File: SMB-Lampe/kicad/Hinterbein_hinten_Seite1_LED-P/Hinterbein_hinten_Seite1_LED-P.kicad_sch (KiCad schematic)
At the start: 10 parts, among them J1 Conn_01x01_Pin, J2 Conn_01x01_Pin, J3 Conn_01x01_Pin, J4 Conn_01x01_Pin, J5 Conn_01x01_Pin, J6 Conn_01x01_Pin

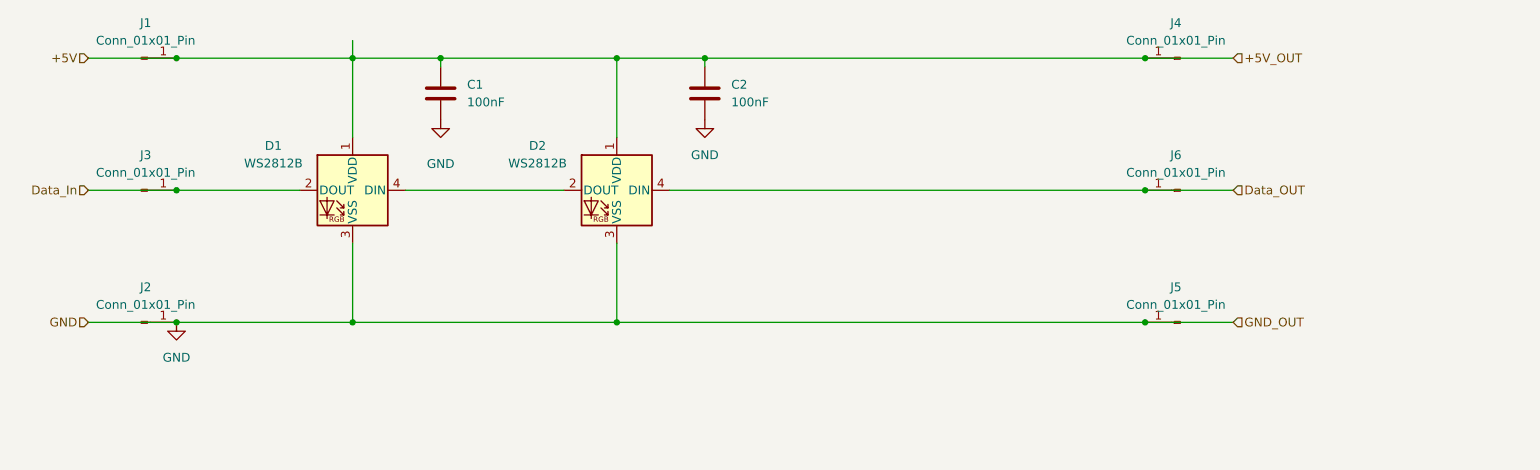
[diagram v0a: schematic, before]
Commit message: Hauptplatine skizziert
Bezeichner stimmen noch nicht
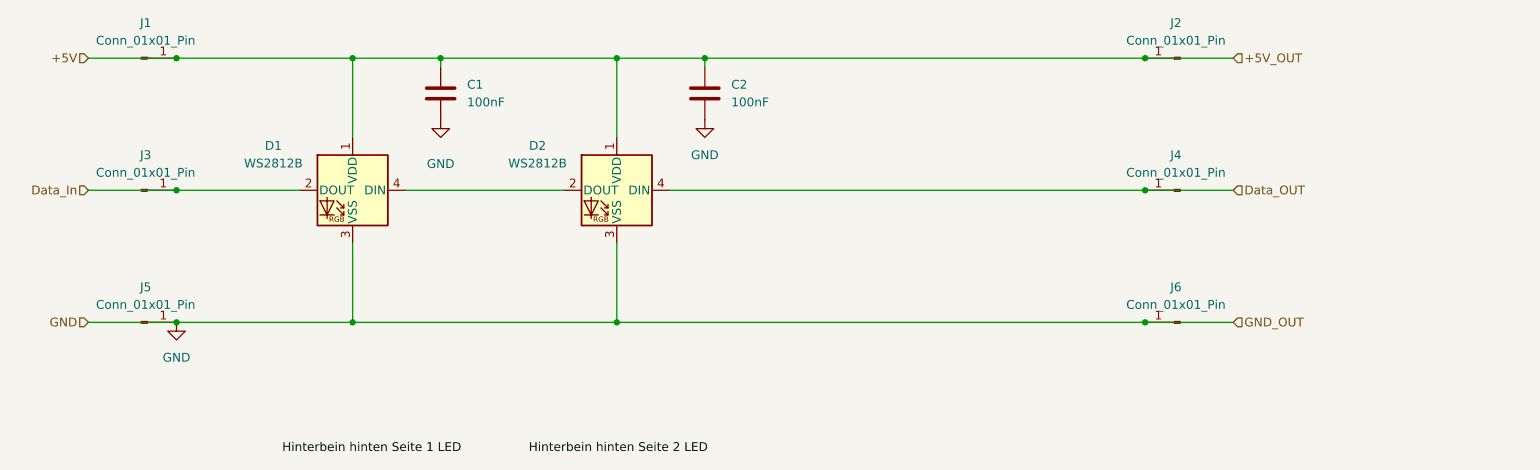
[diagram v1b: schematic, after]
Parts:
- renumbered J4 to J2, J6 to J4, J2 to J5, J5 to J6
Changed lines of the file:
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@@
 	(wire
 		(pts
-			(xy 63.5 22.86) (xy 63.5 25.4)
+			(xy 101.6 63.5) (xy 177.8 63.5)
 		)
 		(stroke
@@
 	(wire
 		(pts
-			(xy 101.6 63.5) (xy 177.8 63.5)
+			(xy 38.1 44.45) (xy 55.88 44.45)
 		)
 		(stroke
@@
 	(wire
 		(pts
-			(xy 38.1 44.45) (xy 55.88 44.45)
+			(xy 101.6 25.4) (xy 101.6 36.83)
 		)
 		(stroke
@@
 	(wire
 		(pts
-			(xy 101.6 25.4) (xy 101.6 36.83)
+			(xy 63.5 25.4) (xy 76.2 25.4)
 		)
 		(stroke
@@
 	(wire
 		(pts
-			(xy 63.5 25.4) (xy 76.2 25.4)
+			(xy 76.2 25.4) (xy 76.2 26.67)
 		)
 		(stroke
@@
 	(wire
 		(pts
-			(xy 76.2 25.4) (xy 76.2 26.67)
+			(xy 114.3 26.67) (xy 114.3 25.4)
 		)
 		(stroke
@@
 	(wire
 		(pts
-			(xy 114.3 26.67) (xy 114.3 25.4)
+			(xy 109.22 44.45) (xy 177.8 44.45)
 		)
 		(stroke
@@
 	(wire
 		(pts
-			(xy 109.22 44.45) (xy 177.8 44.45)
+			(xy 71.12 44.45) (xy 93.98 44.45)
 		)
 		(stroke
@@
 	(wire
 		(pts
-			(xy 71.12 44.45) (xy 93.98 44.45)
+			(xy 63.5 52.07) (xy 63.5 63.5)
 		)
 		(stroke
@@
 		)
 	)
-	(wire
-		(pts
-			(xy 63.5 52.07) (xy 63.5 63.5)
-		)
-		(stroke
-			(width 0)
-			(type default)
+	(label "Hinterbein hinten Seite 1 LED"
+		(at 53.34 82.55 0)
+		(effects
+			(font
+				(size 1.27 1.27)
+			)
+			(justify left bottom)
+		)
+	)
+	(label "Hinterbein hinten Seite 2 LED"
+		(at 88.9 82.55 0)
+		(effects
+			(font
+				(size 1.27 1.27)
+			)
+			(justify left bottom)
 		)
 	)
@@
 		(dnp no)
 		(fields_autoplaced yes)
-		(property "Reference" "J2"
+		(property "Reference" "J5"
 			(at 33.655 58.42 0)
 			(effects
@@
 		)
 		(instances
+			(project "SMB-Lampe"
+				(path "/4831ca1b-de6c-4f01-b2f4-c7955e9e85c5/5b746b9f-02d4-420a-904b-6236dfc25b23"
+					(reference "J5")
+					(unit 1)
+				)
+			)
 			(project ""
 				(path "/a4509e87-5503-4154-8e73-9784c4a4e9d8"
@@
 		(dnp no)
 		(fields_autoplaced yes)
-		(property "Reference" "#PWR0103"
+		(property "Reference" "#PWR05"
 			(at 38.1 69.85 0)
 			(effects
@@
 			(project ""
 				(path "/4831ca1b-de6c-4f01-b2f4-c7955e9e85c5/5b746b9f-02d4-420a-904b-6236dfc25b23"
-					(reference "#PWR04")
+					(reference "#PWR05")
 					(unit 1)
 				)
@@
 		)
 		(instances
+			(project "SMB-Lampe"
+				(path "/4831ca1b-de6c-4f01-b2f4-c7955e9e85c5/5b746b9f-02d4-420a-904b-6236dfc25b23"
+					(reference "J1")
+					(unit 1)
+				)
+			)
 			(project ""
 				(path "/a4509e87-5503-4154-8e73-9784c4a4e9d8"
@@
 			(project "SMB-Lampe"
 				(path "/4831ca1b-de6c-4f01-b2f4-c7955e9e85c5/5b746b9f-02d4-420a-904b-6236dfc25b23"
-					(reference "D3")
+					(reference "D2")
 					(unit 1)
 				)
@@
 		(dnp no)
 		(fields_autoplaced yes)
-		(property "Reference" "J4"
+		(property "Reference" "J2"
 			(at 182.245 20.32 0)
 			(effects
@@
 		)
 		(instances
+			(project "SMB-Lampe"
+				(path "/4831ca1b-de6c-4f01-b2f4-c7955e9e85c5/5b746b9f-02d4-420a-904b-6236dfc25b23"
+					(reference "J2")
+					(unit 1)
+				)
+			)
 			(project ""
 				(path "/a4509e87-5503-4154-8e73-9784c4a4e9d8"
@@
 		)
 		(instances
+			(project "SMB-Lampe"
+				(path "/4831ca1b-de6c-4f01-b2f4-c7955e9e85c5/5b746b9f-02d4-420a-904b-6236dfc25b23"
+					(reference "J3")
+					(unit 1)
+				)
+			)
 			(project ""
 				(path "/a4509e87-5503-4154-8e73-9784c4a4e9d8"
@@
 		(dnp no)
 		(fields_autoplaced yes)
-		(property "Reference" "J6"
+		(property "Reference" "J4"
 			(at 182.245 39.37 0)
 			(effects
@@
 		)
 		(instances
+			(project "SMB-Lampe"
+				(path "/4831ca1b-de6c-4f01-b2f4-c7955e9e85c5/5b746b9f-02d4-420a-904b-6236dfc25b23"
+					(reference "J4")
+					(unit 1)
+				)
+			)
 			(project ""
 				(path "/a4509e87-5503-4154-8e73-9784c4a4e9d8"
@@
 		(on_board yes)
 		(dnp no)
-		(property "Reference" "#PWR0101"
+		(property "Reference" "#PWR03"
 			(at 76.2 40.64 0)
 			(effects
@@
 		(dnp no)
 		(fields_autoplaced yes)
-		(property "Reference" "#PWR0102"
+		(property "Reference" "#PWR04"
 			(at 114.3 40.64 0)
 			(effects
@@
 			(project "SMB-Lampe"
 				(path "/4831ca1b-de6c-4f01-b2f4-c7955e9e85c5/5b746b9f-02d4-420a-904b-6236dfc25b23"
-					(reference "#PWR05")
+					(reference "#PWR04")
 					(unit 1)
 				)
@@
 		(dnp no)
 		(fields_autoplaced yes)
-		(property "Reference" "J5"
+		(property "Reference" "J6"
 			(at 182.245 58.42 0)
 			(effects
@@
 		)
 		(instances
+			(project "SMB-Lampe"
+				(path "/4831ca1b-de6c-4f01-b2f4-c7955e9e85c5/5b746b9f-02d4-420a-904b-6236dfc25b23"
+					(reference "J6")
+					(unit 1)
+				)
+			)
 			(project ""
 				(path "/a4509e87-5503-4154-8e73-9784c4a4e9d8"

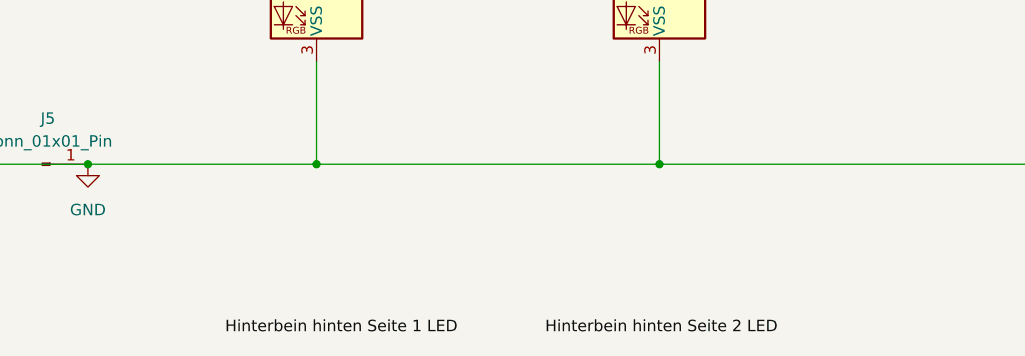
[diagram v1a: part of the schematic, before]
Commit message: Alle Platinen erstellt
Alle Platinen wurden im Projekt einzeln erstellt.
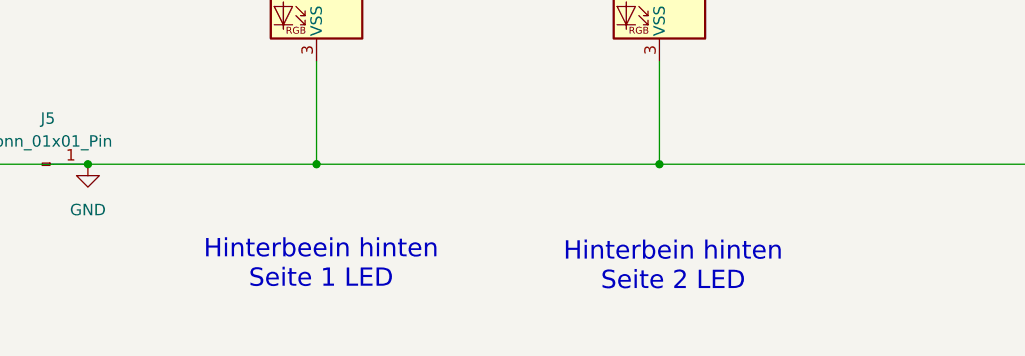
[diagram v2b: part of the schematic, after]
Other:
- note added: "Hinterbeein hinten Seite 1 LED"
- note added: "Hinterbein hinten Seite 2 LED"

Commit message: Alle LEDs nochmal richtig angeschlossen
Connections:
- net Data_In: now also D1.4 (DIN); no longer D1.2 (DOUT)
- net Data_OUT: now also D2.2 (DOUT); no longer D2.4 (DIN)
- new net: D1.2 (DOUT), D2.4 (DIN)
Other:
- moved on the sheet: C1, C2
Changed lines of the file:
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@@
 	)
 	(junction
-		(at 76.2 25.4)
+		(at 52.07 25.4)
 		(diameter 0)
 		(color 0 0 0 0)
@@
 	)
 	(junction
+		(at 90.17 25.4)
+		(diameter 0)
+		(color 0 0 0 0)
+	)
+	(junction
 		(at 38.1 63.5)
 		(diameter 0)
@@
 		(color 0 0 0 0)
 	)
-	(junction
-		(at 114.3 25.4)
-		(diameter 0)
-		(color 0 0 0 0)
-	)
 	(wire
 		(pts
@@
 	(wire
 		(pts
-			(xy 76.2 25.4) (xy 101.6 25.4)
-		)
-		(stroke
-			(width 0)
-			(type default)
-		)
-	)
-	(wire
-		(pts
 			(xy 25.4 25.4) (xy 38.1 25.4)
 		)
@@
 	(wire
 		(pts
-			(xy 38.1 25.4) (xy 63.5 25.4)
+			(xy 38.1 25.4) (xy 52.07 25.4)
 		)
 		(stroke
@@
 	(wire
 		(pts
-			(xy 114.3 25.4) (xy 177.8 25.4)
-		)
-		(stroke
-			(width 0)
-			(type default)
-		)
-	)
-	(wire
-		(pts
 			(xy 177.8 44.45) (xy 190.5 44.45)
 		)
@@
 	(wire
 		(pts
-			(xy 101.6 25.4) (xy 114.3 25.4)
-		)
-		(stroke
-			(width 0)
-			(type default)
-		)
-	)
-	(wire
-		(pts
 			(xy 63.5 25.4) (xy 63.5 36.83)
 		)
@@
 	(wire
 		(pts
-			(xy 63.5 25.4) (xy 76.2 25.4)
-		)
-		(stroke
-			(width 0)
-			(type default)
-		)
-	)
-	(wire
-		(pts
-			(xy 76.2 25.4) (xy 76.2 26.67)
-		)
-		(stroke
-			(width 0)
-			(type default)
-		)
-	)
-	(wire
-		(pts
-			(xy 114.3 26.67) (xy 114.3 25.4)
+			(xy 52.07 25.4) (xy 63.5 25.4)
+		)
+		(stroke
+			(width 0)
+			(type default)
+		)
+	)
+	(wire
+		(pts
+			(xy 63.5 25.4) (xy 90.17 25.4)
+		)
+		(stroke
+			(width 0)
+			(type default)
+		)
+	)
+	(wire
+		(pts
+			(xy 101.6 25.4) (xy 177.8 25.4)
+		)
+		(stroke
+			(width 0)
+			(type default)
+		)
+	)
+	(wire
+		(pts
+			(xy 52.07 25.4) (xy 52.07 27.94)
+		)
+		(stroke
+			(width 0)
+			(type default)
+		)
+	)
+	(wire
+		(pts
+			(xy 90.17 26.67) (xy 90.17 25.4)
+		)
+		(stroke
+			(width 0)
+			(type default)
+		)
+	)
+	(wire
+		(pts
+			(xy 90.17 25.4) (xy 101.6 25.4)
 		)
 		(stroke
@@
 	(symbol
 		(lib_id "Device:C")
-		(at 114.3 30.48 0)
+		(at 90.17 30.48 0)
 		(unit 1)
 		(exclude_from_sim no)
@@
 		(fields_autoplaced yes)
 		(property "Reference" "C2"
-			(at 118.11 29.2099 0)
+			(at 93.98 29.2099 0)
 			(effects
 				(font
@@
 		)
 		(property "Value" "100nF"
-			(at 118.11 31.7499 0)
+			(at 93.98 31.7499 0)
 			(effects
 				(font
@@
 		)
 		(property "Footprint" "Capacitor_SMD:C_0201_0603Metric"
-			(at 115.2652 34.29 0)
+			(at 91.1352 34.29 0)
 			(effects
 				(font
@@
 		)
 		(property "Datasheet" "~"
-			(at 114.3 30.48 0)
+			(at 90.17 30.48 0)
 			(effects
 				(font
@@
 		)
 		(property "Description" "Unpolarized capacitor"
-			(at 114.3 30.48 0)
+			(at 90.17 30.48 0)
 			(effects
 				(font
@@
 	(symbol
 		(lib_id "Device:C")
-		(at 76.2 30.48 0)
+		(at 52.07 31.75 0)
 		(unit 1)
 		(exclude_from_sim no)
@@
 		(fields_autoplaced yes)
 		(property "Reference" "C1"
-			(at 80.01 29.2099 0)
+			(at 55.88 30.4799 0)
 			(effects
 				(font
@@
 		)
 		(property "Value" "100nF"
-			(at 80.01 31.7499 0)
+			(at 55.88 33.0199 0)
 			(effects
 				(font
@@
 		)
 		(property "Footprint" "Capacitor_SMD:C_0201_0603Metric"
-			(at 77.1652 34.29 0)
+			(at 53.0352 35.56 0)
 			(effects
 				(font
@@
 		)
 		(property "Datasheet" "~"
-			(at 76.2 30.48 0)
+			(at 52.07 31.75 0)
 			(effects
 				(font
@@
 		)
 		(property "Description" "Unpolarized capacitor"
-			(at 76.2 30.48 0)
+			(at 52.07 31.75 0)
 			(effects
 				(font
@@
 		(lib_id "LED:WS2812B")
 		(at 101.6 44.45 0)
-		(mirror y)
 		(unit 1)
 		(exclude_from_sim no)
@@
 		(dnp no)
 		(property "Reference" "D2"
-			(at 90.17 38.0298 0)
+			(at 113.03 38.0298 0)
 			(effects
 				(font
@@
 		)
 		(property "Value" "WS2812B"
-			(at 90.17 40.5698 0)
+			(at 113.03 40.5698 0)
 			(effects
 				(font
@@
 		)
 		(property "Footprint" "LED_SMD:LED_WS2812B_PLCC4_5.0x5.0mm_P3.2mm"
-			(at 100.33 52.07 0)
+			(at 102.87 52.07 0)
 			(effects
 				(font
@@
 		)
 		(property "Datasheet" "https://cdn-shop.adafruit.com/datasheets/WS2812B.pdf"
-			(at 99.06 53.975 0)
+			(at 104.14 53.975 0)
 			(effects
 				(font
@@
 	(symbol
 		(lib_id "power:GND")
-		(at 76.2 34.29 0)
+		(at 52.07 35.56 0)
 		(unit 1)
 		(exclude_from_sim no)
@@
 		(dnp no)
 		(property "Reference" "#PWR03"
-			(at 76.2 40.64 0)
+			(at 52.07 41.91 0)
 			(effects
 				(font
@@
 		)
 		(property "Value" "GND"
-			(at 76.2 40.64 0)
+			(at 52.07 41.91 0)
 			(effects
 				(font
@@
 		)
 		(property "Footprint" ""
-			(at 76.2 34.29 0)
+			(at 52.07 35.56 0)
 			(effects
 				(font
@@
 		)
 		(property "Datasheet" ""
-			(at 76.2 34.29 0)
+			(at 52.07 35.56 0)
 			(effects
 				(font
@@
 		)
 		(property "Description" "Power symbol creates a global label with name \"GND\" , ground"
-			(at 76.2 34.29 0)
+			(at 52.07 35.56 0)
 			(effects
 				(font
@@
 	(symbol
 		(lib_id "power:GND")
-		(at 114.3 34.29 0)
+		(at 90.17 34.29 0)
 		(unit 1)
 		(exclude_from_sim no)
@@
 		(fields_autoplaced yes)
 		(property "Reference" "#PWR04"
-			(at 114.3 40.64 0)
+			(at 90.17 40.64 0)
 			(effects
 				(font
@@
 		)
 		(property "Value" "GND"
-			(at 114.3 39.37 0)
+			(at 90.17 39.37 0)
 			(effects
 				(font
@@
 		)
 		(property "Footprint" ""
-			(at 114.3 34.29 0)
+			(at 90.17 34.29 0)
 			(effects
 				(font
@@
 		)
 		(property "Datasheet" ""
-			(at 114.3 34.29 0)
+			(at 90.17 34.29 0)
 			(effects
 				(font
@@
 		)
 		(property "Description" "Power symbol creates a global label with name \"GND\" , ground"
-			(at 114.3 34.29 0)
+			(at 90.17 34.29 0)
 			(effects
 				(font
@@
 		(lib_id "LED:WS2812B")
 		(at 63.5 44.45 0)
-		(mirror y)
 		(unit 1)
 		(exclude_from_sim no)
@@
 		(dnp no)
 		(property "Reference" "D1"
-			(at 52.07 38.0298 0)
+			(at 74.93 38.0298 0)
 			(effects
 				(font
@@
 		)
 		(property "Value" "WS2812B"
-			(at 52.07 40.5698 0)
+			(at 74.93 40.5698 0)
 			(effects
 				(font
@@
 		)
 		(property "Footprint" "LED_SMD:LED_WS2812B_PLCC4_5.0x5.0mm_P3.2mm"
-			(at 62.23 52.07 0)
+			(at 64.77 52.07 0)
 			(effects
 				(font
@@
 		)
 		(property "Datasheet" "https://cdn-shop.adafruit.com/datasheets/WS2812B.pdf"
-			(at 60.96 53.975 0)
-			(effects
-				(font
+			(at 66.04 53.975 0)
+			(effects
+				(font

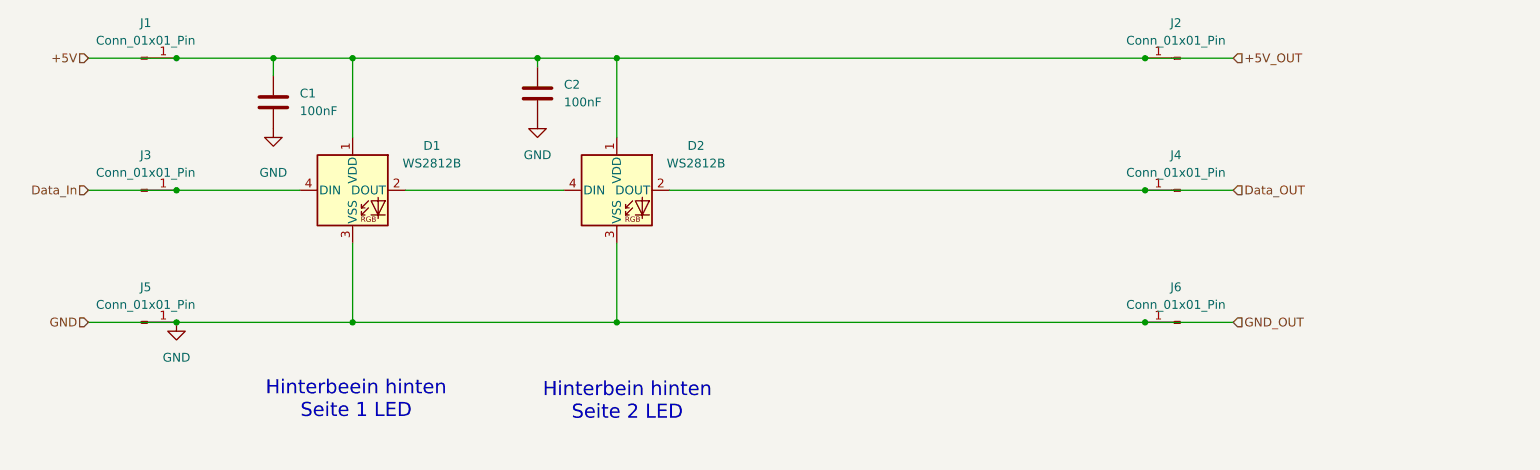
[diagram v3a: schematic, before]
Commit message: Hinterbein Seite 1/2 erstellt
Anschlüsse zwischen den Platinen mit MountingHoles. Eigenes MountingHole Erstellt
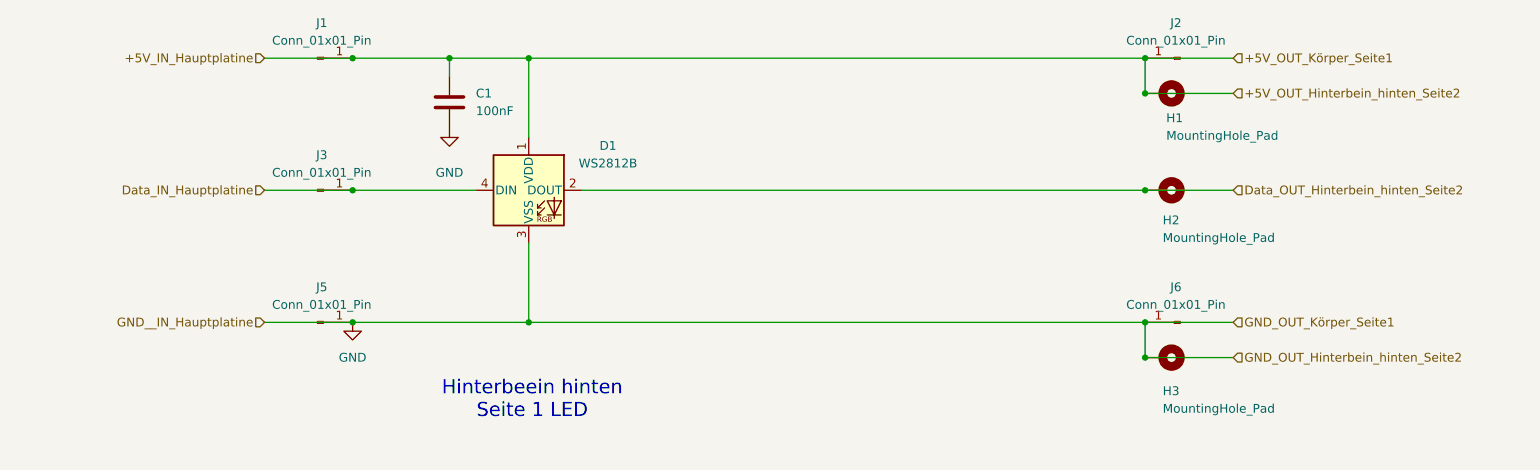
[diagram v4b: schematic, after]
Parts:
- removed C2: 100nF, Capacitor_SMD:C_0201_0603Metric, symbol Device:C
- removed D2: WS2812B, LED_SMD:LED_WS2812B_PLCC4_5.0x5.0mm_P3.2mm, symbol LED:WS2812B
- removed J4: Conn_01x01_Pin, TestPoint:TestPoint_Pad_1.0x1.0mm, symbol Connector:Conn_01x01_Pin
- added H1, H2, H3: MountingHole_Pad, Eigenen_Library:MountingHole D2,5 x d1 test, symbol Mechanical:MountingHole_Pad
- J1, J2, J3, J5, J6: footprint TestPoint:TestPoint_Pad_1.0x1.0mm -> TestPoint:TestPoint_Pad_2.0x2.0mm
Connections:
- net GND: now also H3.1
- net Data_OUT_Hinterbein_hinten_Seite2: now reaches D1.2 (DOUT)
- net Data_OUT_Hinterbein_hinten_Seite2: now also H2.1
- net +5V renamed +5V_IN_Hauptplatine
- net +5V_IN_Hauptplatine: now also H1.1
- net Data_In renamed Data_IN_Hauptplatine
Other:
- note removed: "Hinterbein hinten Seite 2 LED"
- moved on the sheet: C1, D1, J1, J3, J5

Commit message: Hinterbein Hinten fertig
Seite 1 und Seite 2 von Hinterbein hinten Sind fertig
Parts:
- H1, H2, H3: footprint Eigenen_Library:MountingHole D2,5 x d1 test -> Eigenen_Library:MountingHole D2 x d1 test
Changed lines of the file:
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@@
 			)
 		)
-		(property "Footprint" "Eigenen_Library:MountingHole D2,5 x d1 test"
+		(property "Footprint" "Eigenen_Library:MountingHole D2 x d1 test"
 			(at 180.34 44.45 0)
 			(effects
@@
 			)
 		)
-		(property "Footprint" "Eigenen_Library:MountingHole D2,5 x d1 test"
+		(property "Footprint" "Eigenen_Library:MountingHole D2 x d1 test"
 			(at 180.34 30.48 0)
 			(effects
@@
 			)
 		)
-		(property "Footprint" "Eigenen_Library:MountingHole D2,5 x d1 test"
+		(property "Footprint" "Eigenen_Library:MountingHole D2 x d1 test"
 			(at 180.34 68.58 0)
 			(effects

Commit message: Vorderseite Platine Körper Seite 1 fertig
zwei GND Verbindungen fehlen noch
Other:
- note added: "Hinterbein hinten Seite 1 LED"
- note removed: "Hinterbeein hinten Seite 1 LED"
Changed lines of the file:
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@@
 	(generator_version "9.0")
 	(paper "A4")
-	(text "Hinterbeein hinten\nSeite 1 LED"
+	(text "Hinterbein hinten\nSeite 1 LED"
 		(exclude_from_sim no)
 		(at 89.408 74.676 0)

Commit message: Vorderes Hinterbein fertig
Alle Platinen sind fertig beschaltet
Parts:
- renumbered J5 to J2, J2 to J4, J6 to J5
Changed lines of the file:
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@@
 		(dnp no)
 		(fields_autoplaced yes)
-		(property "Reference" "J5"
+		(property "Reference" "J2"
 			(at 59.055 58.42 0)
 			(effects
@@
 		(dnp no)
 		(fields_autoplaced yes)
-		(property "Reference" "#PWR05"
+		(property "Reference" "#PWR0103"
 			(at 63.5 69.85 0)
 			(effects
@@
 				)
 			)
+			(project "Hinterbein_hinten_Seite1_LED-P"
+				(path "/a4509e87-5503-4154-8e73-9784c4a4e9d8"
+					(reference "H2")
+					(unit 1)
+				)
+			)
 		)
 	)
@@
 				)
 			)
+			(project "Hinterbein_hinten_Seite1_LED-P"
+				(path "/a4509e87-5503-4154-8e73-9784c4a4e9d8"
+					(reference "H1")
+					(unit 1)
+				)
+			)
 		)
 	)
@@
 			(project ""
 				(path "/4831ca1b-de6c-4f01-b2f4-c7955e9e85c5/5b746b9f-02d4-420a-904b-6236dfc25b23"
+					(reference "H3")
+					(unit 1)
+				)
+			)
+			(project "Hinterbein_hinten_Seite1_LED-P"
+				(path "/a4509e87-5503-4154-8e73-9784c4a4e9d8"
 					(reference "H3")
 					(unit 1)
@@
 		(on_board yes)
 		(dnp no)
-		(property "Reference" "J2"
+		(property "Reference" "J4"
 			(at 182.245 20.32 0)
 			(effects
@@
 		(on_board yes)
 		(dnp no)
-		(property "Reference" "#PWR03"
+		(property "Reference" "#PWR0101"
 			(at 77.47 41.91 0)
 			(effects
@@
 		(dnp no)
 		(fields_autoplaced yes)
-		(property "Reference" "J6"
+		(property "Reference" "J5"
 			(at 182.245 58.42 0)
 			(effects
